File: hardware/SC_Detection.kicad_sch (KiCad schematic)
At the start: 86 parts, among them U15 LT1678CS8#PBF, U16 LT1678CS8#PBF, U17 LM211DRG4, U18 LM211DRG4, U19 LM211DRG4, U20 LM211DRG4

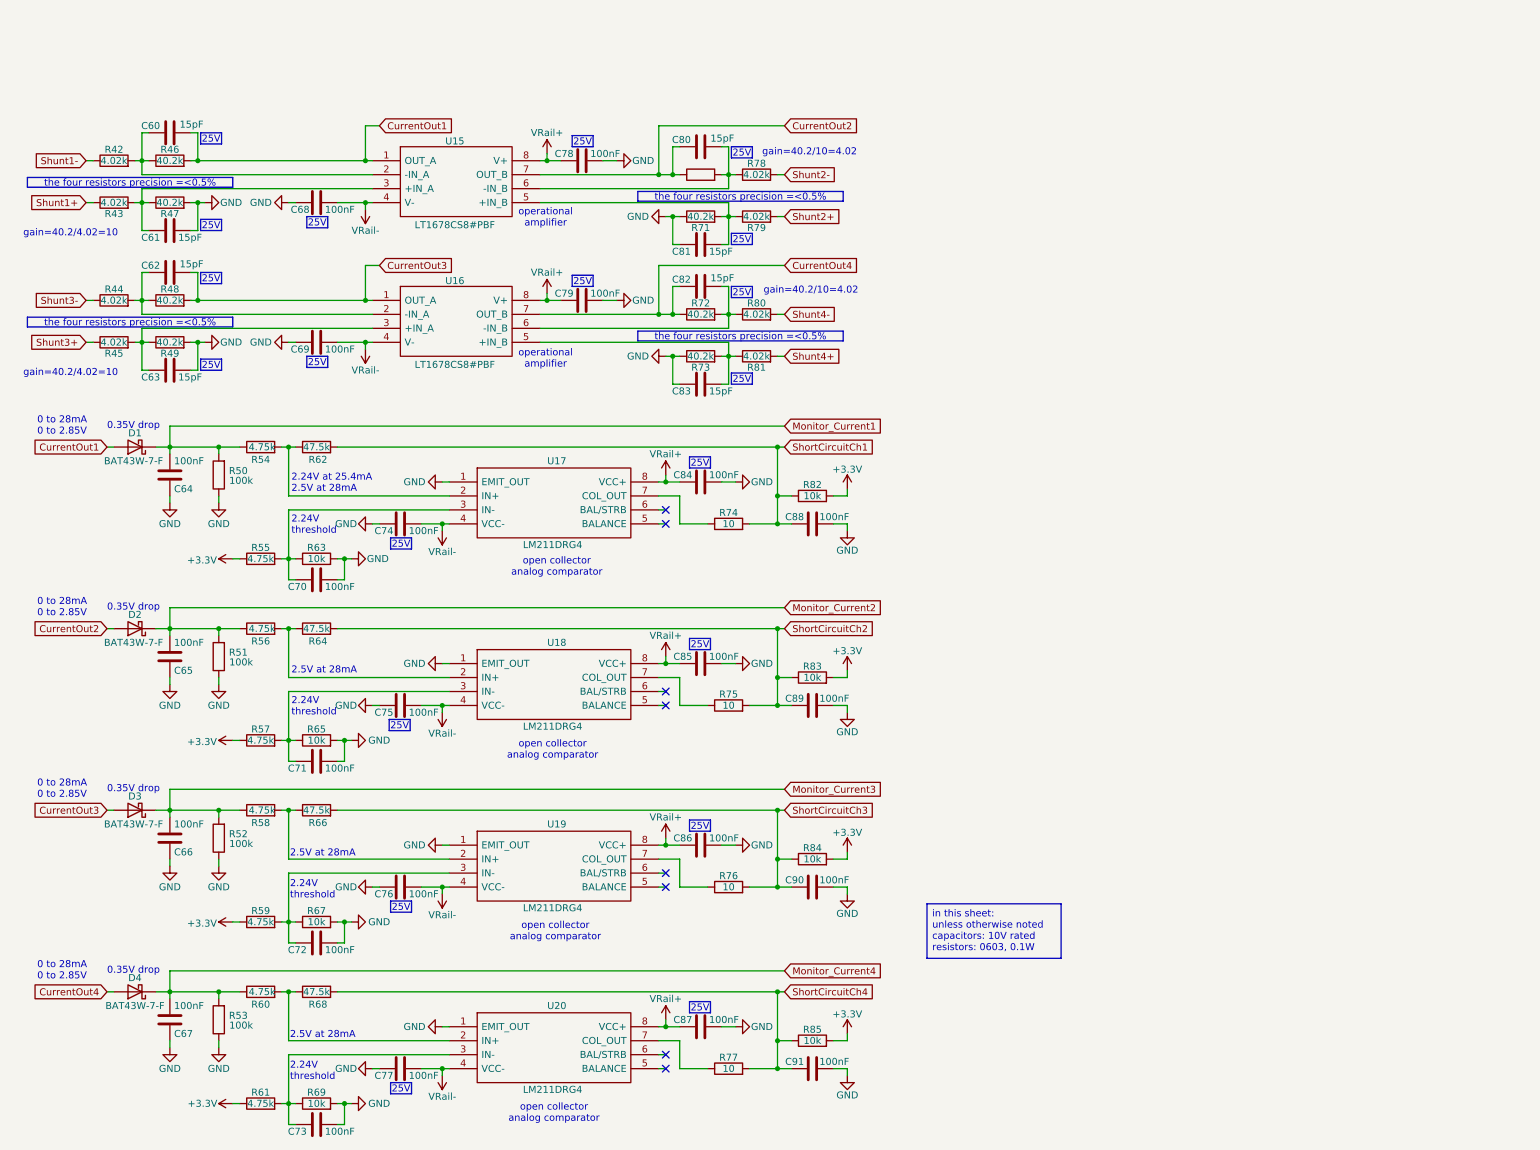
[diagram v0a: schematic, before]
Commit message: draft new analog signal chain & short-circuit detection
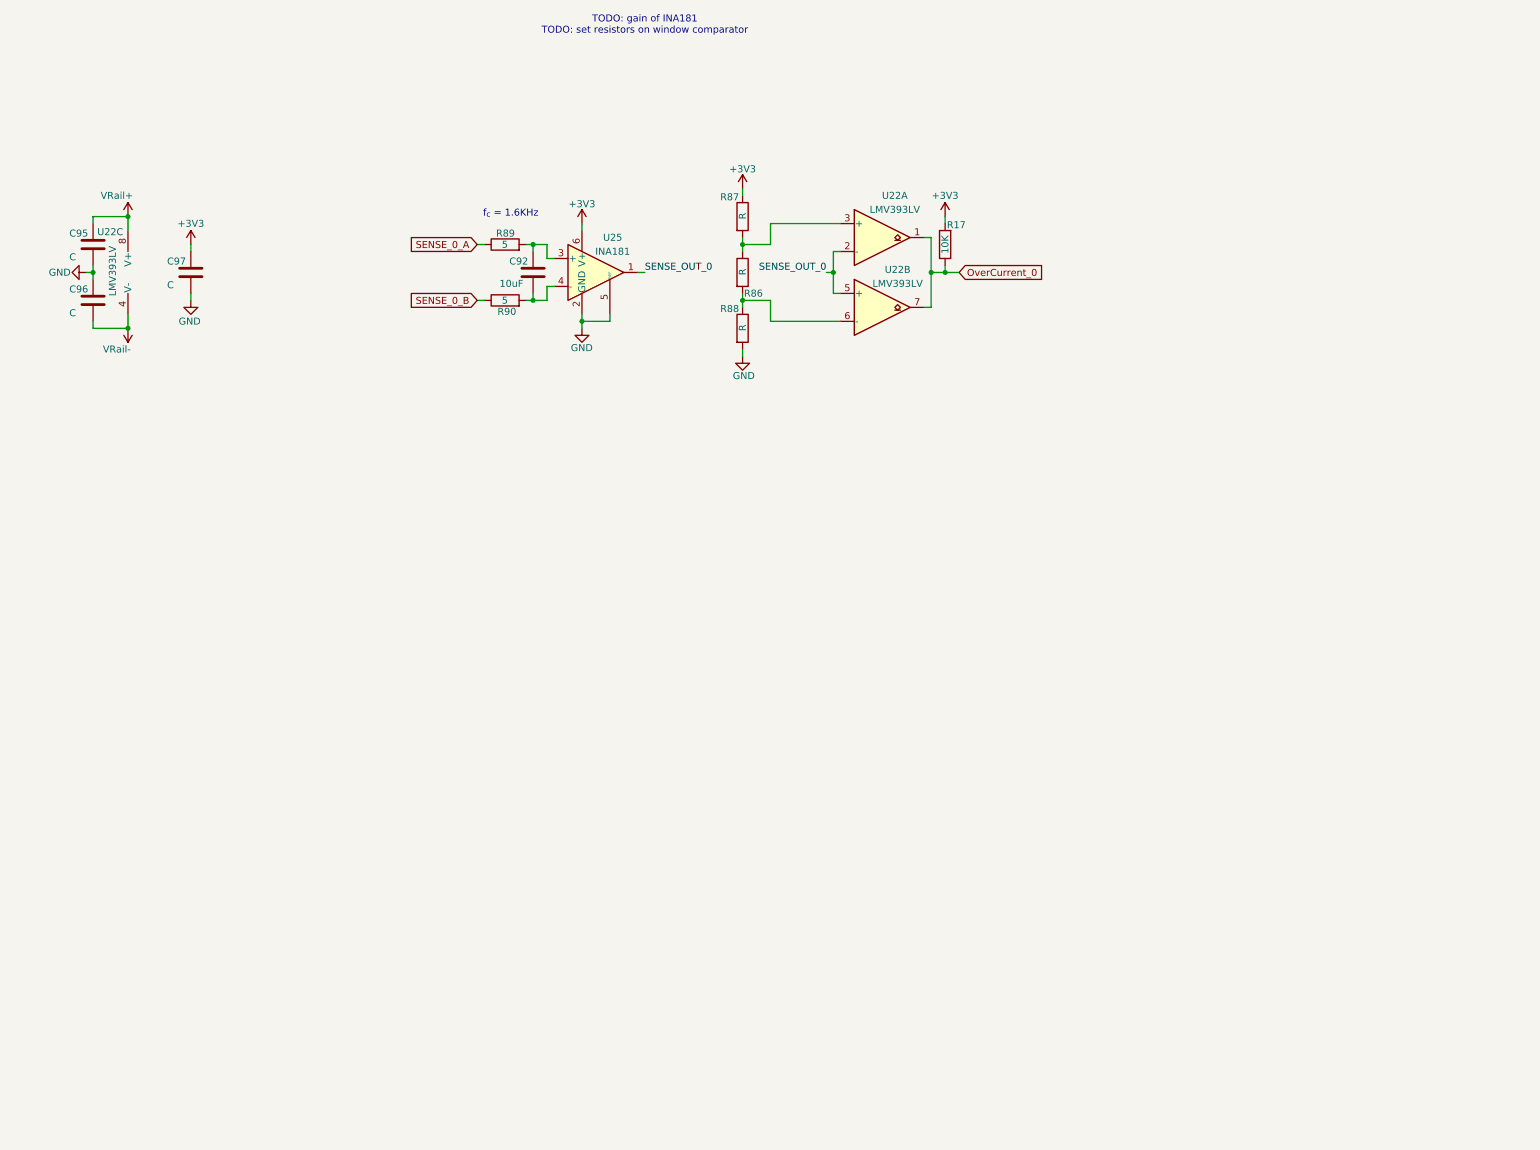
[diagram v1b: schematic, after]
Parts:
- removed C60, C61, C62, C63, C80, C81, C82, C83: 15pF, Capacitor_SMD:C_0603_1608Metric, symbol harp.device.quad.dac:C_0603
- removed C64, C65, C66, C67, C68, C69, C70, C71, C72, C73, C74, C75, C76, C77, C78, C79, C84, C85, C86, C87, C88, C89, C90, C91: 100nF, Capacitor_SMD:C_0603_1608Metric, symbol harp.device.quad.dac:C_0603
- removed D1, D2, D3, D4: BAT43W-7-F, Diode_SMD:D_SOD-123, symbol harp.device.quad.dac:BAT43W-V
- removed R42, R43, R44, R45, R78, R79, R80, R81: 4.02k, Resistor_SMD:R_0603_1608Metric, symbol harp.device.quad.dac:R_0603
- removed R46, R47, R48, R49, R70, R71, R72, R73: 40.2k, Resistor_SMD:R_0603_1608Metric, symbol harp.device.quad.dac:R_0603
- removed R50, R51, R52, R53: 100k, Resistor_SMD:R_0603_1608Metric, symbol harp.device.quad.dac:R_0603
- removed R54, R55, R56, R57, R58, R59, R60, R61: 4.75k, Resistor_SMD:R_0603_1608Metric, symbol harp.device.quad.dac:R_0603
- removed R62, R64, R66, R68: 47.5k, Resistor_SMD:R_0603_1608Metric, symbol harp.device.quad.dac:R_0603
- removed R63, R65, R67, R69, R82, R83, R84, R85: 10k, Resistor_SMD:R_0603_1608Metric, symbol harp.device.quad.dac:R_0603
- removed R74, R75, R76, R77: 10, Resistor_SMD:R_0603_1608Metric, symbol harp.device.quad.dac:R_0603
- removed U15, U16: LT1678CS8#PBF, harp.device.quad.dac.kicad:SOIC127P599X175-8N, symbol harp.device.quad.dac:LT1678CS8#PBF
- removed U17, U18, U19, U20: LM211DRG4, harp.device.quad.dac.kicad:SOIC127P600X175-8N, symbol harp.device.quad.dac:LM211DRG4
- added C92: 10uF, symbol Device:C
- added C95, C96, C97: C, symbol Device:C
- added R17: 10K, symbol Device:R
- added R86, R87, R88: R, symbol Device:R
- added R89, R90: 5, symbol Device:R
- added U22: LMV393LV, symbol Comparator:LMV393
- added U25: INA181, Package_TO_SOT_SMD:SOT-23-6, symbol Amplifier_Current:INA181
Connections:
- net GND: now also C95.2, C96.1, C97.2, R88.2, U25.2 (GND), U25.5 (REF)
- net VRail+: now also C95.1, U22.8 (V+)
- net VRail-: now also C96.2, U22.4 (V-)
- new net: C92.1, R89.2, U25.3 (+)
- new net: C92.2, R90.2, U25.4 (-)
- new net: R86.1, R87.2, U22.3 (+)
- new net: R86.2, R88.1, U22.6 (-)
- new net +3V3: C97.1, R17.2, R87.1, U25.6 (V+)
- new net OverCurrent_0: R17.1, U22.1, U22.7
- new net SENSE_0_A: R89.1
- new net SENSE_0_B: R90.1
- new net SENSE_OUT_0: U22.2 (-), U22.5 (+), U25.1
- no-connect marks 8 -> 0
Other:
- note added: "TODO: gain of INA181 TODO: set resistors on window comparator"
- note added: "f_{c} = 1.6KHz"
- note removed: "0 to 28mA 0 to 2.85V"
- note removed: "0.35V drop"
- note removed: "2.24V at 25.4mA"
- note removed: "2.24V threshold"
- note removed: "2.5V at 28mA"
- note removed: "gain=40.2/10=4.02"
- note removed: "gain=40.2/4.02=10"
- note removed: "open collector analog comparator"
- note removed: "operational amplifier"

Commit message: draft split rail power supply design
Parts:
- removed C96: C, symbol Device:C
- added C39, C41, C44, C46, C50, C52, C54: 100nF, symbol Device:C
- added C42, C47, C53: 10uF, symbol Device:C
- added R24, R26, R31, R32, R37, R38: 5, symbol Device:R
- added R27, R29, R30, R33, R35, R36, R39, R41, R42: 10K, symbol Device:R
- added R28, R34, R40: 40K, symbol Device:R
- added U11: REF2033, Package_TO_SOT_SMD:SOT-23-5, symbol kicad_component_library:REF20xx
- added U12, U15, U17: LMV393LV, symbol Comparator:LMV393
- added U13, U16, U18: INA181, Package_TO_SOT_SMD:SOT-23-6, symbol Amplifier_Current:INA181
- C92: Link (none) -> https://www.digikey.com/en/products/detail/samsung-electro-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; Manufacturer (none) -> Samsung Electro-Mechanics; Manufacturer Number (none) -> CL10A106MA8NRNC
- C95, C97: value C -> 100nF
- R86: value R -> 40K
- R87, R88: value R -> 10K
- U25: Manufacturer (none) -> Texas Instruments; Manufacturer Number (none) -> INA181A4
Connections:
- net VRail+ is gone; now on net +3V3: C95.1, U22.8 (V+)
- net VRail- is gone; now on net GND: U22.4 (V-)
- net +3V3: now also C39.1, C41.1, C44.1, C46.1, C50.1, C52.1, C54.1, R27.1, R30.2, R33.1, R36.2, R39.1, R42.2, U12.8 (V+), U13.6 (V+), U15.8 (V+), U16.6 (V+), U17.8 (V+), U18.6 (V+)
- net GND: now also C39.2, C41.2, C44.2, C46.2, C50.2, C52.2, C54.2, R29.2, R35.2, R41.2, U11.2 (GND), U12.4 (V-), U13.2 (GND), U15.4 (V-), U16.2 (GND), U17.4 (V-), U18.2 (GND); no longer U25.5 (REF)
- net SENSE_OUT_0: now also U12.2 (-), U12.5 (+), U13.1, U15.2 (-), U15.5 (+), U16.1, U17.2 (-), U17.5 (+), U18.1
- new net: R27.2, R28.1, U12.3 (+)
- new net: R28.2, R29.1, U12.6 (-)
- new net: C53.1, R37.2, U18.3 (+)
- new net: C53.2, R38.2, U18.4 (-)
- new net: R40.2, R41.1, U17.6 (-)
- new net: R33.2, R34.1, U15.3 (+)
- new net: C42.1, R24.2, U13.3 (+)
- new net: R39.2, R40.1, U17.3 (+)
- new net: C47.1, R31.2, U16.3 (+)
- new net: C47.2, R32.2, U16.4 (-)
- new net: R34.2, R35.1, U15.6 (-)
- new net: C42.2, R26.2, U13.4 (-)
- new net +5V: U11.3 (EN), U11.4 (VIN)
- new net OverCurrent_1: R30.1, U12.1, U12.7
- new net OverCurrent_2: R36.1, U15.1, U15.7
- new net OverCurrent_3: R42.1, U17.1, U17.7
- new net SENSE_1_A: R24.1
- new net SENSE_1_B: R26.1
- new net SENSE_2_A: R31.1
- new net SENSE_2_B: R32.1
- new net SENSE_3_A: R37.1
- new net SENSE_3_B: R38.1
- new net VREF_1V65: U11.1 (VBIAS), U13.5 (REF), U16.5 (REF), U18.5 (REF), U25.5 (REF)
- new net VREF_3V3: U11.5 (VREF)
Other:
- note added: "Dual Voltage Reference"
- note added: "G = 200 I_{max} = 125mA R_{sense} = 0.05 V_{ref} = 1.65V"
- note added: "VREF can source up to 20mA."
- note added: "V_{max} = 2.75V ∴ I_{max} = 110mA"
- note added: "V_{min} = 0.55V ∴ I_{min} = -110mA"
- note added: "V_{out} = 200·I_{load}R_{sense} + V_{ref}"
- note removed: "TODO: gain of INA181 TODO: set resistors on window comparator"
- moved on the sheet: C92, C95, C97, R17, R86, R87, R88, R89, R90, U22A, U22B, U22C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

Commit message: add note in schematic
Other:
- note added: "Bidirectional Current Sensing + Window Comparator"
- moved on the sheet: C39, C41, C42, C44, C46, C47, C50, C52, C53, C92, C95, C97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

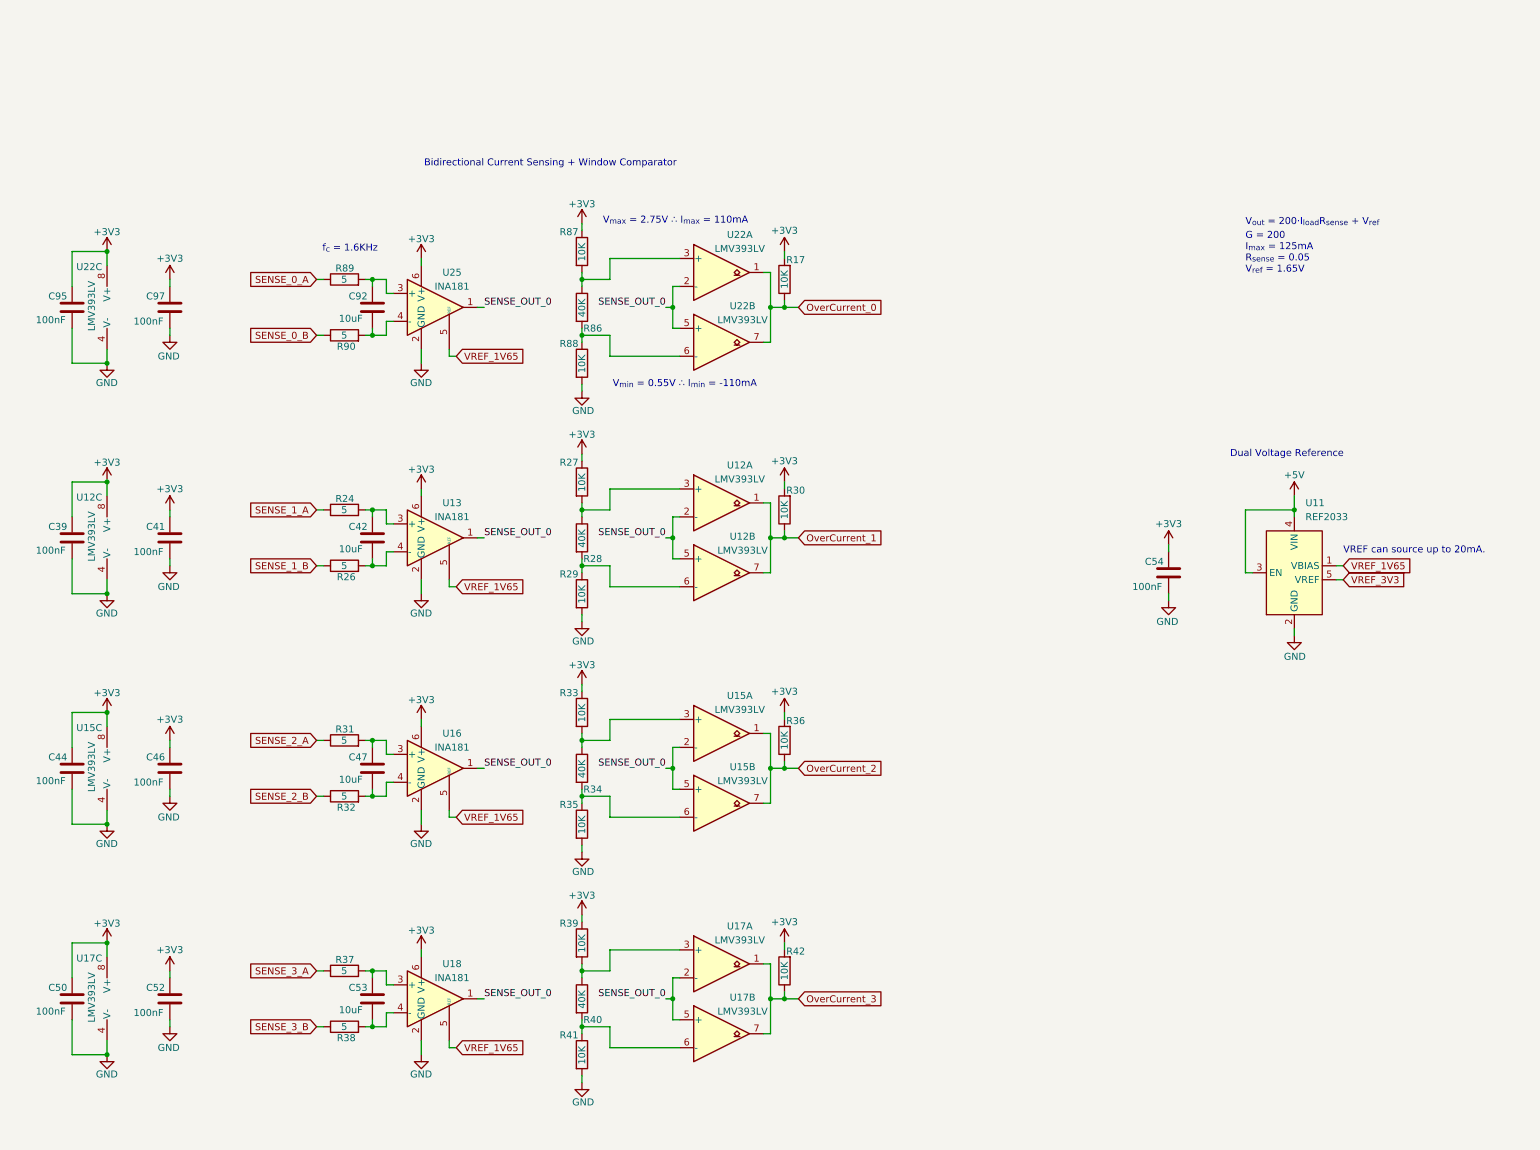
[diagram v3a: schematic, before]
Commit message: update tvs diodes, regulators, and power supply chain
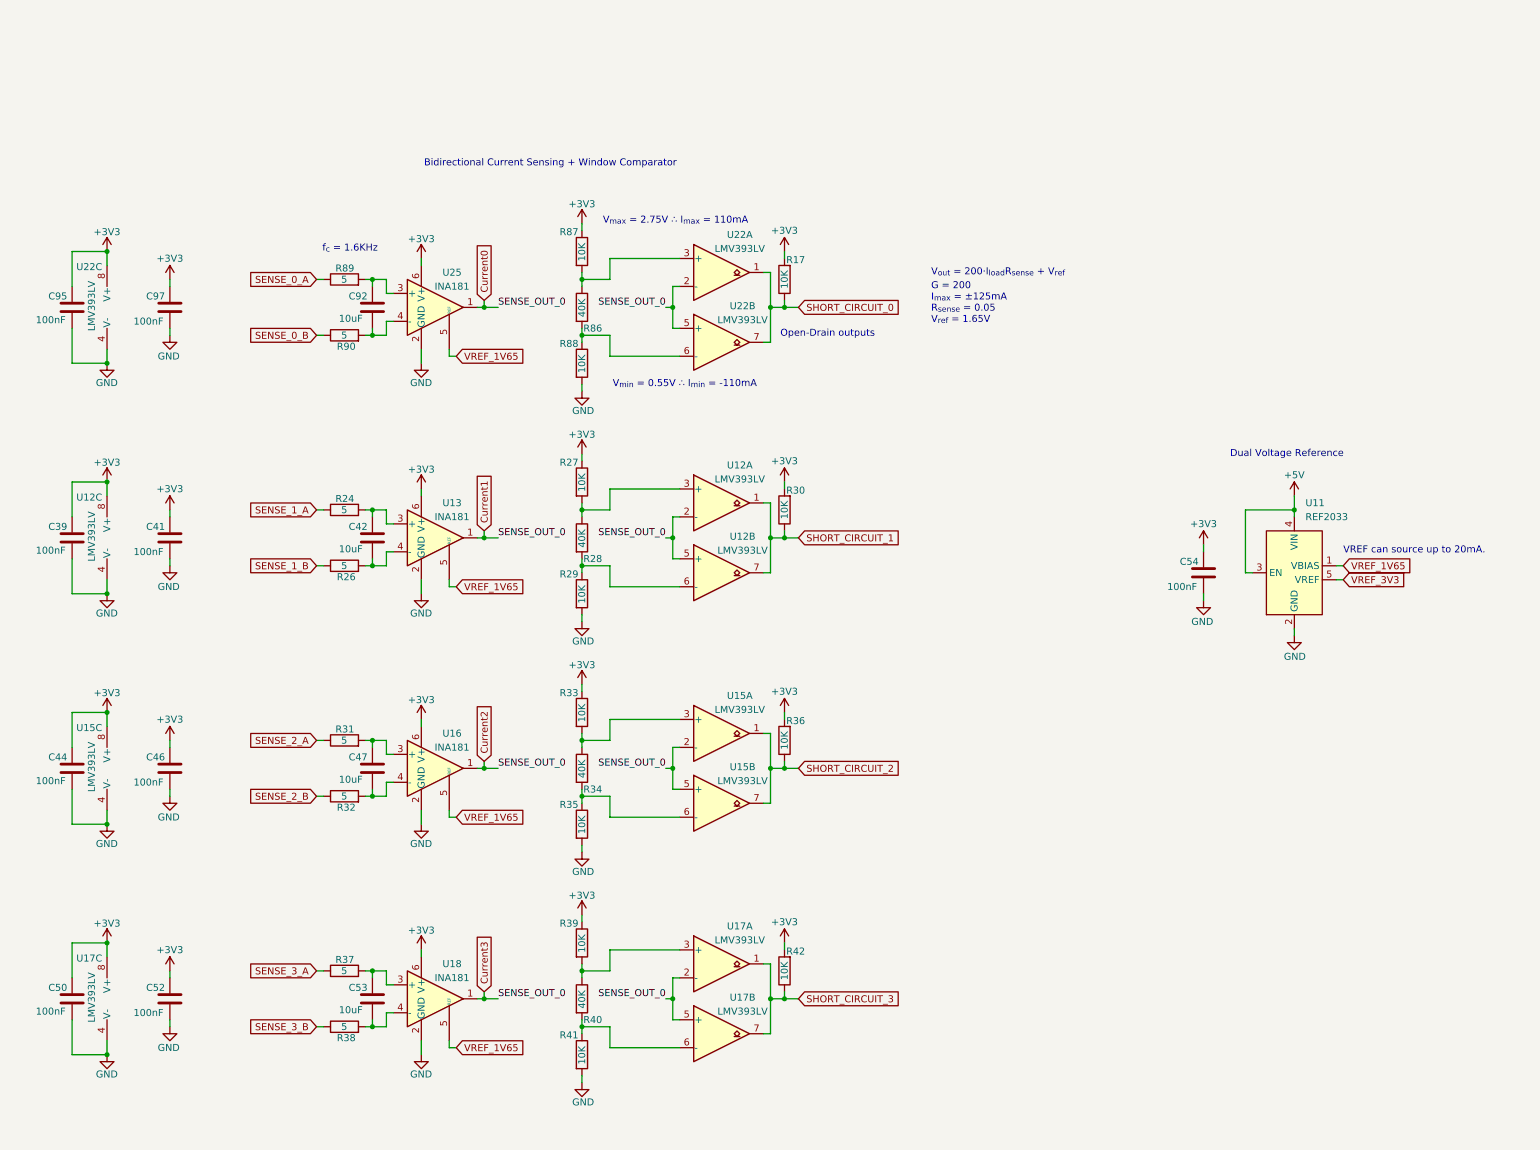
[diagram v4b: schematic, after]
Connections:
- net OverCurrent_0 renamed SHORT_CIRCUIT_0
- net OverCurrent_1 renamed SHORT_CIRCUIT_1
- net OverCurrent_2 renamed SHORT_CIRCUIT_2
- net OverCurrent_3 renamed SHORT_CIRCUIT_3
- net SENSE_OUT_0 renamed Current0
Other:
- note added: "G = 200 I_{max} = ±125mA R_{sense} = 0.05 V_{ref} = 1.65V"
- note added: "Open-Drain outputs"
- note removed: "G = 200 I_{max} = 125mA R_{sense} = 0.05 V_{ref} = 1.65V"
- moved on the sheet: C54
